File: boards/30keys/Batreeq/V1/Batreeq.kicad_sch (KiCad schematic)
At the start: 96 parts, among them J1 Conn_01x12_Female, J2 Conn_01x12_Female, SW1 SW_Push, SW10 SW_Push, SW11 SW_Push, SW12 SW_Push, SW13 SW_Push, SW14 SW_Push, SW15 SW_Push, SW16 SW_Push, SW17 SW_Push, SW18 SW_Push, SW19 SW_Push, SW2 SW_Push, SW20 SW_Push, SW21 SW_Push, SW22 SW_Push, SW23 SW_Push, SW24 SW_Push, SW25 SW_Push, SW26 SW_Push, SW27 SW_Push, SW28 SW_Push, SW29 SW_Push, SW3 SW_Push, SW30 SW_Push, SW31 SW_Push, SW32 SW_Push, SW33 SW_Push, SW34 SW_Push, SW35 SW_Push, SW36 RotaryEncoder, SW37 SW_SPDT, SW4 SW_Push, SW5 SW_Push, SW6 SW_Push, SW7 SW_Push, SW8 SW_Push, SW9 SW_Push, U2 74HC595, U3 TCR2EF19,LM(CT, U4 PMW3360DM-T2QU, U5 DRV2605L

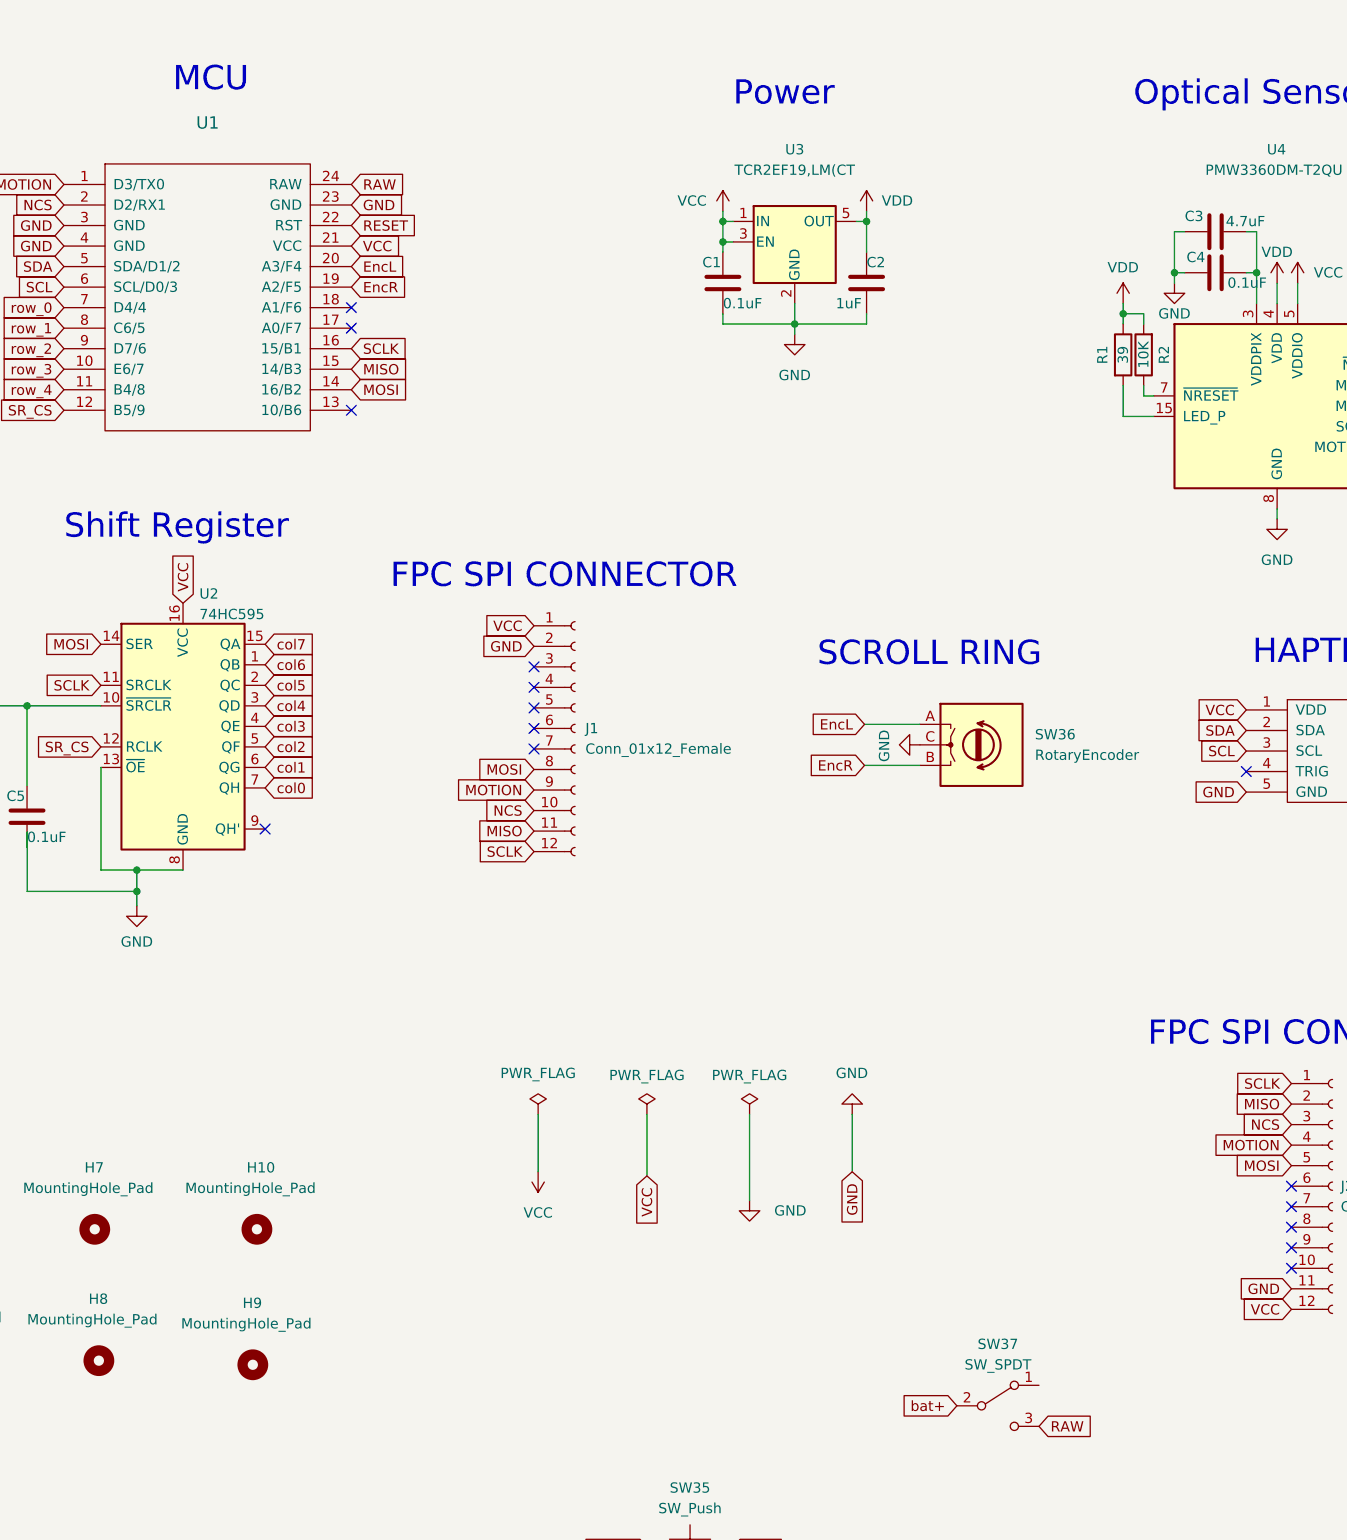
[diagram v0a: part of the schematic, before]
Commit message: add resistors to scroll ring circuit
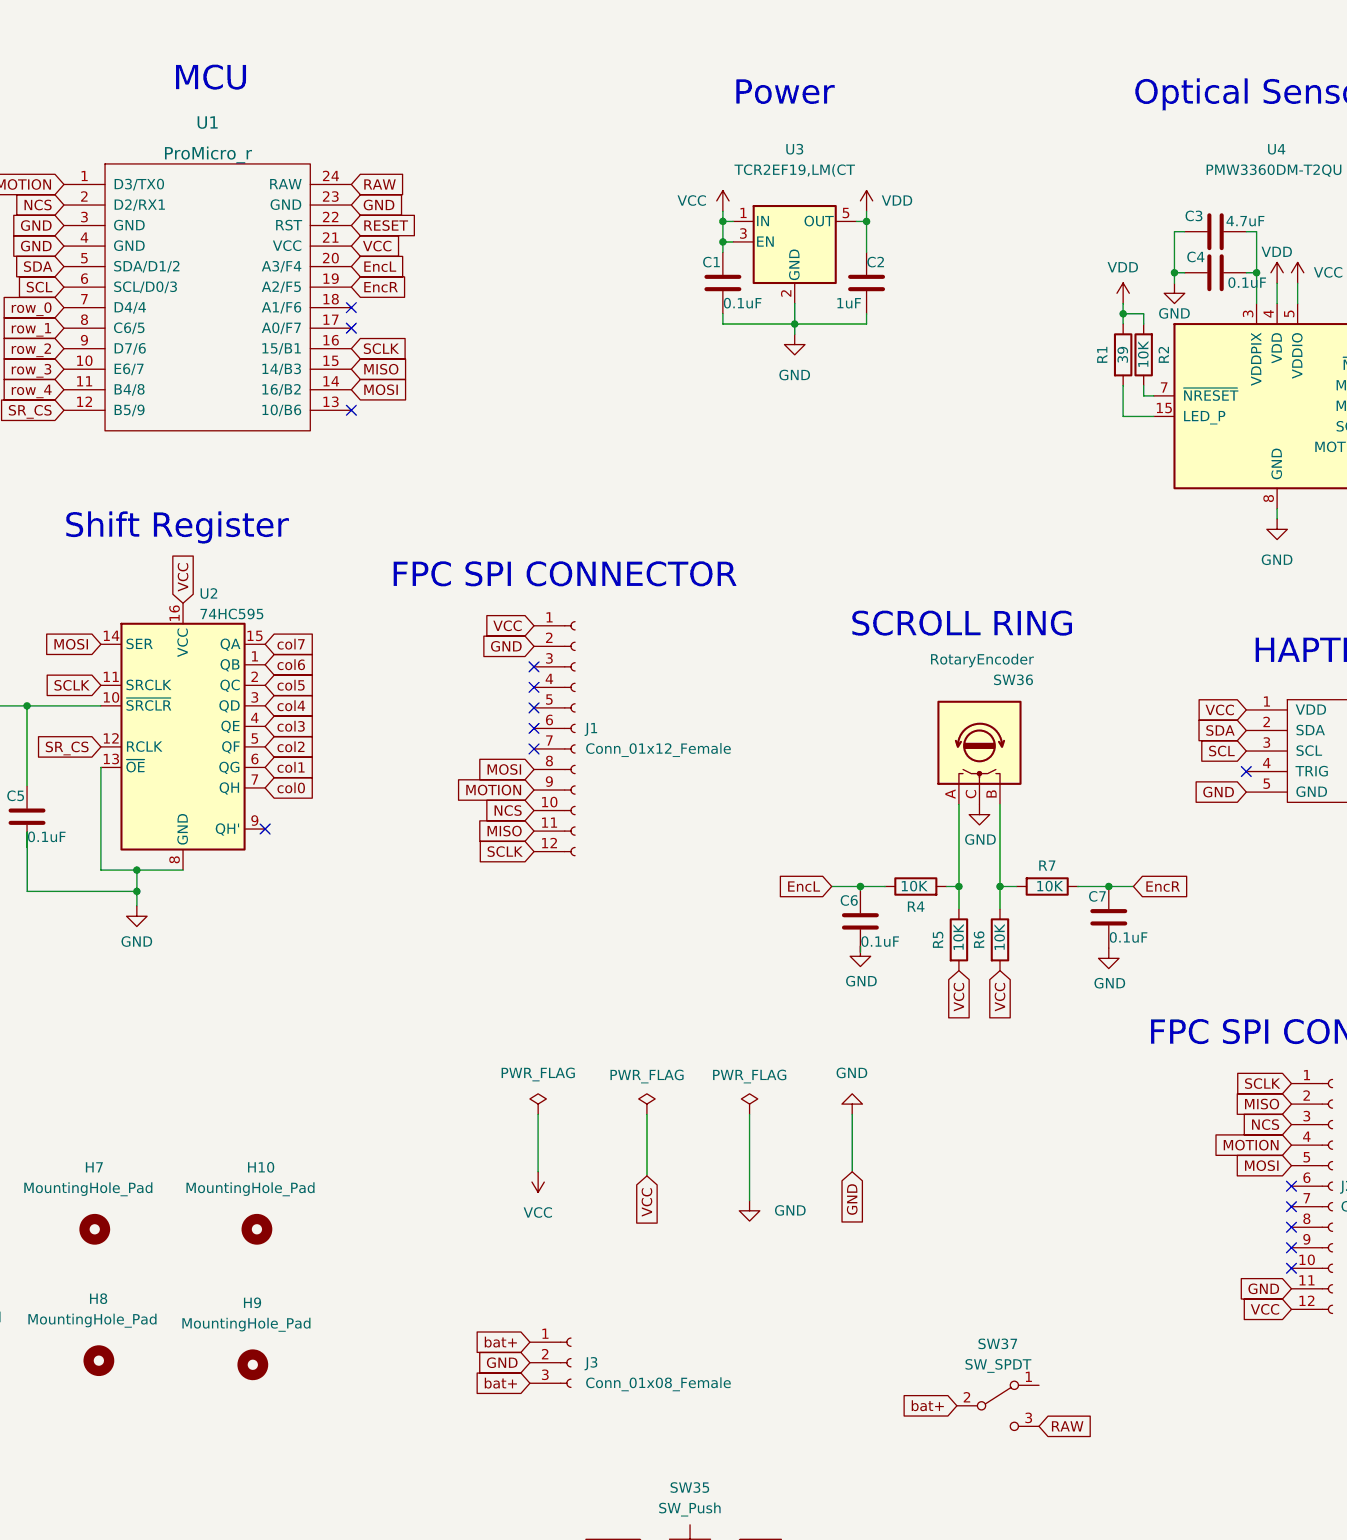
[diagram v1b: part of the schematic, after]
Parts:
- added C6, C7: 0.1uF, Capacitor_SMD:C_0805_2012Metric, symbol Device:C
- added J3: Conn_01x08_Female, Alaa:3JST_BAT, symbol Connector:Conn_01x03_Female
- added R4, R5, R6, R7: 10K, Resistor_SMD:R_0805_2012Metric, symbol Device:R
- U1: value (none) -> ProMicro_r; footprint (none) -> Alaa:ProMicro2
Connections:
- net EncL: now also C6.1, R4.1; no longer SW36.A
- net EncR: now also C7.1, R7.1; no longer SW36.B
- net GND: now also C6.2, C7.2, J3.2 (Pin_2)
- net VCC: now also R5.2, R6.2
- net bat+: now also J3.1 (Pin_1), J3.3 (Pin_3)
- new net: R4.2, R5.1, SW36.A
- new net: R6.1, R7.2, SW36.B
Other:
- moved on the sheet: SW36
